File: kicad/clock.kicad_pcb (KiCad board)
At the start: 4 copper layers, 110 x 110 mm, 189 parts, among them J1 GCT_USB4160-03-0230-C_USB_C_V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, J10 JST_ZH_B6B-ZR_1x06_P1.50mm_Ve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, J11 JST_ZH_B2B-ZR_1x02_P1.50mm_Ve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, J2 PinHeader_1x04_P2.54mm_Vertic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, J3 JST_PH_B2B-PH-K_1x02_P2.00mm_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, J6 microSD_HC_Hirose_DM3AT-SF-PE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, J7 JST_ZH_B6B-ZR_1x06_P1.50mm_Ve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, J9 JST_PH_B3B-PH-K_1x03_P2.00mm_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, M1 Juken_X40-879_DualShaft, Q1 SOT-23, Q2 SOT-23, Q3 SOT-23, Q4 SOT-23, Q6 SOT-23, Q7 SOT-23, SW1 SW_SPST_CK_RS282G05A3, SW2 SW_SPST_CK_RS282G05A3, U1 TSSOP-10_3x3mm_P0.5mm, U10 SOT-23-6, U11 SSOP-24_5.3x8.2mm_P0.65mm, U12 SSOP-24_5.3x8.2mm_P0.65mm, U13 SSOP-28_5.3x10.2mm_P0.65mm, U14 OnSemi_QRE1113GR, U15 SOT-23-5, U2 MSOP-12-1EP_3x4.039mm_P0.65mm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, U3 SOT-23-6, U4 SOIC-8_3.9x4.9mm_P1.27mm, U5 SOT-563, U6 SOT-23-5, U7 Texas_HTSSOP-14-1EP_4.4x5mm_P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, U8 ESP32-S3-WROOM-1, U9 HTSSOP-32-1EP_6.1x11mm_P0.65m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, Y1 Crystal_SMD_3215-2Pin_3.2x1.5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

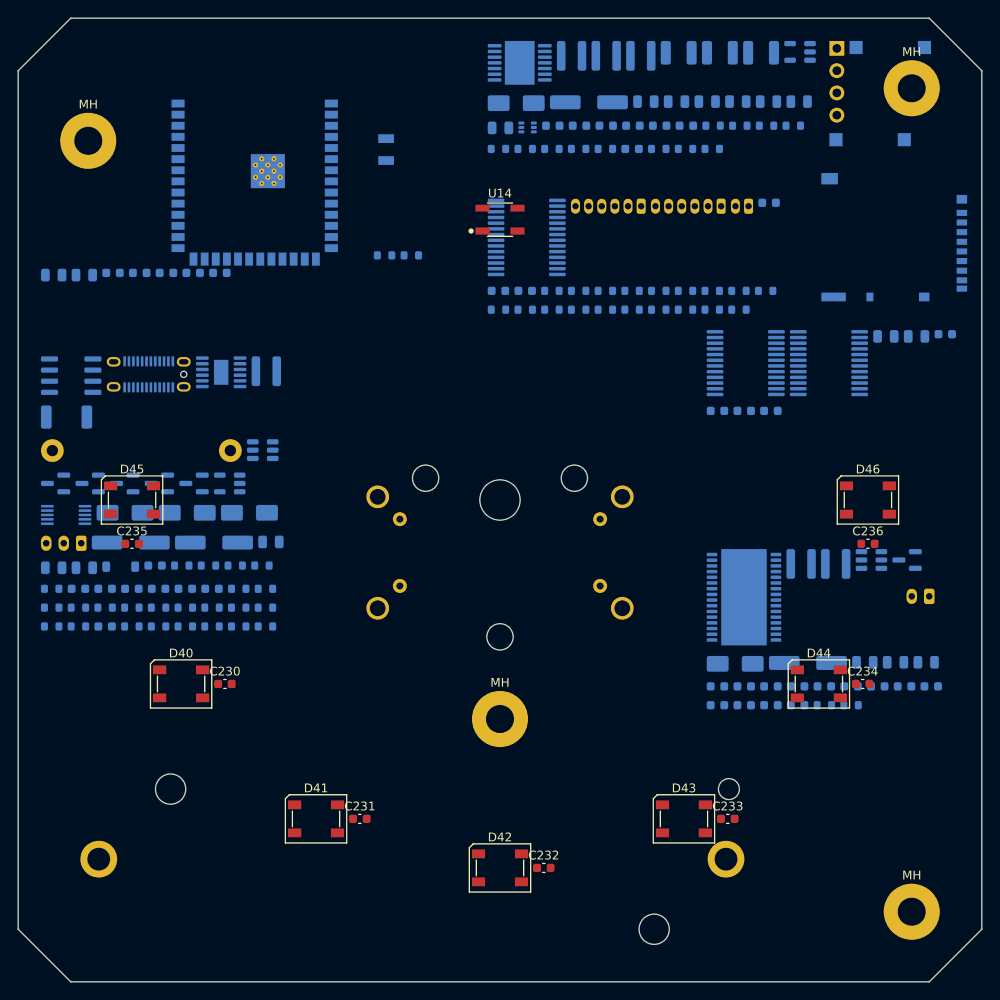
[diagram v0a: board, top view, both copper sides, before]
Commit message: fix PCB layout
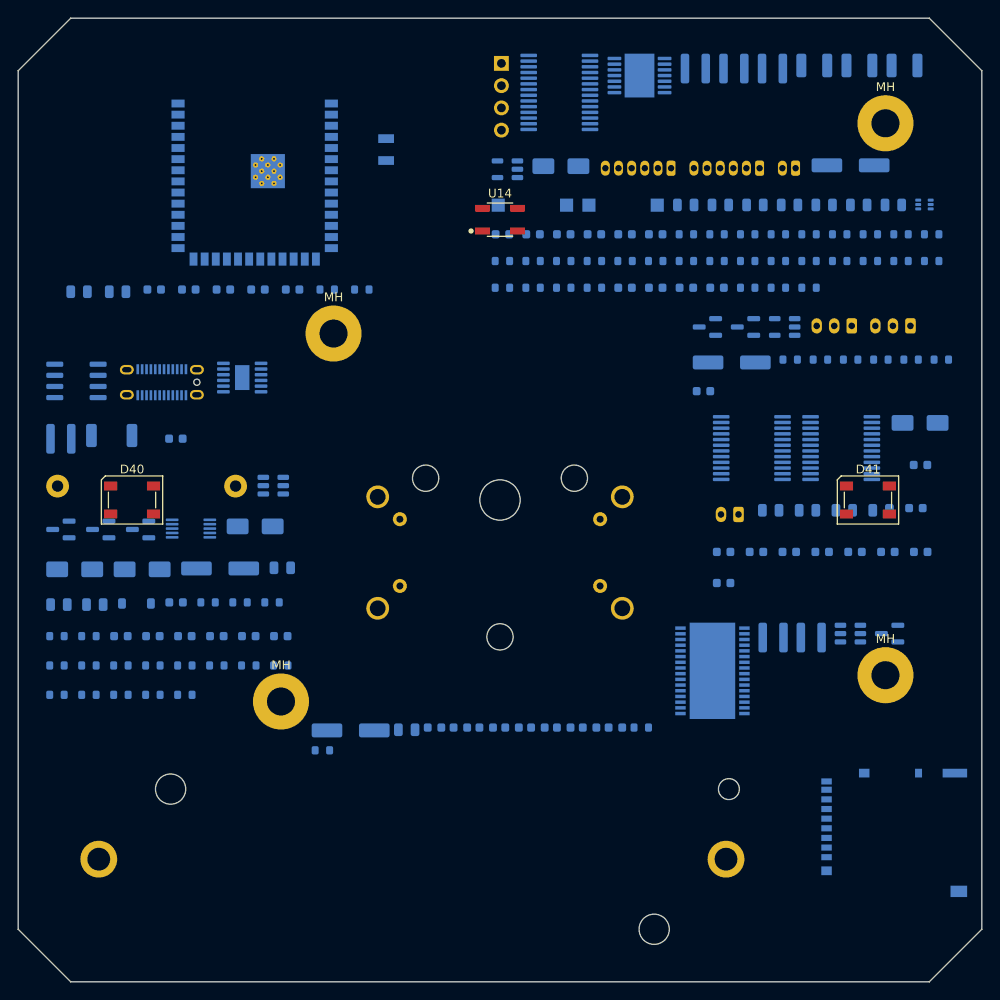
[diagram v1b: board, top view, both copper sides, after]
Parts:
- removed C232, C233, C234, C235, C236: C_0603_1608Metric, C_0603_1608Metric
- removed D42, D43, D44, D45, D46: LED_SK6812_PLCC4_5.0x5.0mm_P3.2mm, LED_SK6812_PLCC4_5.0x5.0mm_P3.2mm
- removed the MH at (8.00, 14.0)
- removed the MH at (102.0, 8.00)
- removed the MH at (55.0, 80.0)
- removed the MH at (102.0, 102.0)
- removed the R97 at (85.3, 31.1)
- removed the R97 at (76.2, 33.3)
- removed the R98 at (54.8, 33.3)
- removed the R98 at (79.2, 33.3)
- removed the R99 at (82.3, 33.3)
- removed the R99 at (57.9, 33.3)
- added J12: JST_PH_B3B-PH-K_1x03_P2.00mm_Vertical, JST_PH_B3B-PH-K_1x03_P2.00mm_Vertical, B.Cu at (101.8, 35.1)
- added MH: MountingHole_3.2mm_M3_Pad, MountingHole_3.2mm_M3_Pad, F.Cu at (36.0, 36.0)
- added MH: MountingHole_3.2mm_M3_Pad, MountingHole_3.2mm_M3_Pad, F.Cu at (99.0, 75.0)
- added MH: MountingHole_3.2mm_M3_Pad, MountingHole_3.2mm_M3_Pad, F.Cu at (30.0, 78.0)
- added MH: MountingHole_3.2mm_M3_Pad, MountingHole_3.2mm_M3_Pad, F.Cu at (99.0, 12.0)
- added R97: R_0603_1608Metric, R_0603_1608Metric, B.Cu at (58.8, 27.7)
- added R97: R_0603_1608Metric, R_0603_1608Metric, B.Cu at (93.8, 27.7)
- added R98: R_0603_1608Metric, R_0603_1608Metric, B.Cu at (97.3, 27.7)
- added R98: R_0603_1608Metric, R_0603_1608Metric, B.Cu at (62.3, 27.7)
- added R99: R_0603_1608Metric, R_0603_1608Metric, B.Cu at (100.8, 27.7)
- added R99: R_0603_1608Metric, R_0603_1608Metric, B.Cu at (65.8, 27.7)
- C230, C231: moved to B.Cu
- moved J9 91.4 mm to (95.1, 35.1)
- moved R110 82.9 mm to (105.4, 39.0)
- moved R107 82.6 mm to (101.9, 39.0)
- moved R106 82.2 mm to (98.5, 39.0)
- moved R105 81.8 mm to (95.0, 39.0)
- moved R104 81.5 mm to (91.6, 39.0)
- moved R52 81.1 mm to (88.1, 39.0)
- moved C231 75.7 mm to (103.0, 51.0), turned to 180 degrees
- moved C238 73.4 mm to (78.2, 42.6)
- moved D41 72.8 mm to (97.0, 55.0)
- moved J6 68.0 mm to (100.0, 93.0), turned to -90 degrees
- moved U15 65.8 mm to (87.5, 35.2)
- moved Q7 65.4 mm to (83.0, 35.2)
- moved Q6 65.0 mm to (78.7, 35.2)
- moved C237 62.6 mm to (81.5, 39.3)
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
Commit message: pcb creation
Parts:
- removed MH (x4): MountingHole_3.2mm_M3_Pad, MountingHole_3.2mm_M3_Pad
- removed the R97 at (58.8, 27.7)
- removed the R97 at (93.8, 27.7)
- removed the R98 at (97.3, 27.7)
- removed the R98 at (62.3, 27.7)
- removed the R99 at (100.8, 27.7)
- removed the R99 at (65.8, 27.7)
- added C163: C_0603_1608Metric, C_0603_1608Metric, B.Cu at (84.8, 75.9)
- added D13: D_SOD-123, D_SOD-123, B.Cu at (99.1, 104.3)
- added H1: MountingHole_3.2mm_M3_Pad, MountingHole_3.2mm_M3_Pad, F.Cu at (5.00, 5.00)
- added H2: MountingHole_3.2mm_M3_Pad, MountingHole_3.2mm_M3_Pad, F.Cu at (104.8, 5.20)
- added H3: MountingHole_3.2mm_M3_Pad, MountingHole_3.2mm_M3_Pad, F.Cu at (5.00, 105.0)
- added H4: MountingHole_3.2mm_M3_Pad, MountingHole_3.2mm_M3_Pad, F.Cu at (105.5, 105.5)
- added Q8: SOT-23, SOT-23, B.Cu at (100.8, 97.3)
- added Q9: SOT-23, SOT-23, B.Cu at (96.7, 97.3)
- added R24: R_0603_1608Metric, R_0603_1608Metric, B.Cu at (93.4, 61.4)
- added R25: R_0603_1608Metric, R_0603_1608Metric, B.Cu at (95.5, 104.5)
- added R26: R_0603_1608Metric, R_0603_1608Metric, B.Cu at (96.3, 107.9)
- added R27: R_0603_1608Metric, R_0603_1608Metric, B.Cu at (92.7, 108.1)
- added R63: R_0603_1608Metric, R_0603_1608Metric, B.Cu at (85.0, 29.0)
- added R97: R_0603_1608Metric, R_0603_1608Metric, B.Cu at (89.5, 13.8)
- added R98: R_0603_1608Metric, R_0603_1608Metric, B.Cu at (50.4, 31.8)
- added R99: R_0603_1608Metric, R_0603_1608Metric, B.Cu at (54.1, 31.8)
- added U16: SOT-23-6, SOT-23-6, B.Cu at (87.0, 23.7)
- C230, C231: moved to F.Cu
- U1: value TSSOP-10_3x3mm_P0.5mm -> SSOP-10-1EP_3.9x4.9mm_P1mm_EP2.1x3.3mm; footprint TSSOP-10_3x3mm_P0.5mm -> SSOP-10-1EP_3.9x4.9mm_P1mm_EP2.1x3.3mm
- moved C101 103.5 mm to (104.0, 38.1), turned to -90 degrees
- moved R10 103.1 mm to (103.7, 46.0)
- moved J6 103.0 mm to (13.5, 37.0), turned to 90 degrees
- moved R11 97.8 mm to (102.5, 48.3)
- moved C102 96.6 mm to (104.0, 42.0), turned to -90 degrees
- moved C125 95.5 mm to (9.50, 69.5)
- moved U5 95.2 mm to (14.0, 54.0)
- moved R13 94.6 mm to (106.6, 48.5), turned to -90 degrees
- moved R12 93.8 mm to (102.5, 50.4)
- moved R4 92.2 mm to (92.5, 43.3)
- moved Q2 91.5 mm to (92.6, 96.5), turned to -90 degrees
- moved Q3 91.2 mm to (92.5, 104.7), turned to -90 degrees
- moved R43 90.7 mm to (10.0, 73.0)
- moved R19 90.7 mm to (92.0, 100.6), turned to -90 degrees
- moved D12 90.2 mm to (99.2, 92.9)
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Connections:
- J1 pad A6: USB_DP -> Net-(J1-D+-PadA6)
- J1 pad A7: USB_DM -> Net-(J1-D--PadA7)
- J1 pad B6: USB_DP -> Net-(J1-D+-PadA6)
- J1 pad B7: USB_DM -> Net-(J1-D--PadA7)
- U13 pad 8: unconnected-(U13-GPB7-Pad8) -> CELL_TEST
- U7 pad 11: unconnected-(U7-NC-Pad11) -> GND
- U7 pad 7: Net-(U7-COMP) -> GND
- U7 pad 8: GND -> Net-(U7-COMP)
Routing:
- added copper zone on B.Cu, net GND
- added copper zone on F.Cu, net GND
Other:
- board text added: "12V"
- board text added: "3V3"
- board text added: "5V"
- board text added: "AUDIO"
- board text added: "CELL+"
- board text added: "CELL-"
- board text added: "CHARGER"
- board text added: "IO-EXP"
- board text added: "PROTECT"
- board text added: "USB-PD"
- board text added: "WAKE"
- board text added: "clock v0.19"
- board text added: "wooden clock v0.19 2026-07-22"

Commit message: add datasheet and review schematics
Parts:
- BT1: value BatteryHolder_Keystone_1043_1x18650 -> 18650 (Keystone 1043); footprint BatteryHolder_Keystone_1043_1x18650 -> clock:BatteryHolder_Keystone_1043_1x18650
- C1, C108, C144, C160, C165, C167, C171: value C_0603_1608Metric -> 1uF; footprint C_0603_1608Metric -> Capacitor_SMD:C_0603_1608Metric
- C100, C101, C106, C120, C124, C127, C140, C162, C200, C210, C222: value C_0805_2012Metric -> 10uF; footprint C_0805_2012Metric -> Capacitor_SMD:C_0805_2012Metric
- C102, C104, C109, C110, C128, C134, C142, C143, C161, C163, C164, C166, C170, C186, C201, C202, C211, C212, C223, C230, C231, C238, C239, C240, C241: value C_0603_1608Metric -> 100nF; footprint C_0603_1608Metric -> Capacitor_SMD:C_0603_1608Metric
- C105: value C_0603_1608Metric -> 22pF; footprint C_0603_1608Metric -> Capacitor_SMD:C_0603_1608Metric
- C107, C129, C237: value CP_Elec_6.3x7.7 -> 100uF; footprint CP_Elec_6.3x7.7 -> Capacitor_SMD:CP_Elec_6.3x7.7
- C121, C122, C125, C141: value C_0805_2012Metric -> 22uF; footprint C_0805_2012Metric -> Capacitor_SMD:C_0805_2012Metric
- C123: value C_0603_1608Metric -> 220pF; footprint C_0603_1608Metric -> Capacitor_SMD:C_0603_1608Metric
- C126: value C_0603_1608Metric -> 6.8pF; footprint C_0603_1608Metric -> Capacitor_SMD:C_0603_1608Metric
- C130, C131, C132: value C_1210_3225Metric -> 22uF; footprint C_1210_3225Metric -> Capacitor_SMD:C_1210_3225Metric
- C133: value C_0603_1608Metric -> 47nF; footprint C_0603_1608Metric -> Capacitor_SMD:C_0603_1608Metric
- C135: value C_0603_1608Metric -> 100pF; footprint C_0603_1608Metric -> Capacitor_SMD:C_0603_1608Metric
- C145, C146: value C_0603_1608Metric -> 18pF; footprint C_0603_1608Metric -> Capacitor_SMD:C_0603_1608Metric
- C172: value CP_Elec_6.3x7.7 -> 220uF; footprint CP_Elec_6.3x7.7 -> Capacitor_SMD:CP_Elec_6.3x7.7
- C180, C181, C182, C183: value C_0603_1608Metric -> 220nF; footprint C_0603_1608Metric -> Capacitor_SMD:C_0603_1608Metric
- C184, C185: value C_0805_2012Metric -> 0.68uF; footprint C_0805_2012Metric -> Capacitor_SMD:C_0805_2012Metric
- D1: value D_SMA -> SMAJ22CA; footprint D_SMA -> Diode_SMD:D_SMA
- D10: value D_SOD-123 -> BAT46; footprint D_SOD-123 -> Diode_SMD:D_SOD-123
- D11, D20: value D_SMA -> B340A; footprint D_SMA -> Diode_SMD:D_SMA
- D12: value D_SMA -> SMAJ5.0CA; footprint D_SMA -> Diode_SMD:D_SMA
- D13: value D_SOD-123 -> BAT42W; footprint D_SOD-123 -> Diode_SMD:D_SOD-123
- D30: value D_SMA -> SS34; footprint D_SMA -> Diode_SMD:D_SMA
- D40, D41: value LED_SK6812_PLCC4_5.0x5.0mm_P3.2mm -> SK6812RGBW; footprint LED_SK6812_PLCC4_5.0x5.0mm_P3.2mm -> LED_SMD:LED_SK6812_PLCC4_5.0x5.0mm_P3.2mm
- F1: value Fuse_TCO_Cantherm_SDF_L10.5mm_D4.0mm_P20.32mm_Horizontal -> TCO 77C; footprint Fuse_TCO_Cantherm_SDF_L10.5mm_D4.0mm_P20.32mm_Horizontal -> clock:Fuse_TCO_Cantherm_SDF_L10.5mm_D4.0mm_P20.32mm_Horizontal
- J1: value GCT_USB4160-03-0230-C_USB_C_Vertical -> USB4160-03-0230-C; footprint GCT_USB4160-03-0230-C_USB_C_Vertical -> clock:GCT_USB4160-03-0230-C_USB_C_Vertical
- J10: value JST_ZH_B6B-ZR_1x06_P1.50mm_Vertical -> Knob: EM14 enc+SW (top face); footprint JST_ZH_B6B-ZR_1x06_P1.50mm_Vertical -> Connector_JST:JST_ZH_B6B-ZR_1x06_P1.50mm_Vertical
- J11: value JST_ZH_B2B-ZR_1x02_P1.50mm_Vertical -> Radio-off toggle (rear); footprint JST_ZH_B2B-ZR_1x02_P1.50mm_Vertical -> Connector_JST:JST_ZH_B2B-ZR_1x02_P1.50mm_Vertical
- J12: value JST_PH_B3B-PH-K_1x03_P2.00mm_Vertical -> NeoPixel ext (5V/DATA/GND, pos 3-7); footprint JST_PH_B3B-PH-K_1x03_P2.00mm_Vertical -> Connector_JST:JST_PH_B3B-PH-K_1x03_P2.00mm_Vertical
- J2: value PinHeader_1x04_P2.54mm_Vertical -> PROG; footprint PinHeader_1x04_P2.54mm_Vertical -> Connector_PinHeader_2.54mm:PinHeader_1x04_P2.54mm_Vertical
- J3: value JST_PH_B2B-PH-K_1x02_P2.00mm_Vertical -> Speaker DMA58-4 (4R); footprint JST_PH_B2B-PH-K_1x02_P2.00mm_Vertical -> Connector_JST:JST_PH_B2B-PH-K_1x02_P2.00mm_Vertical
- J6: value microSD_HC_Hirose_DM3AT-SF-PEJM5 -> DM3AT-SF-PEJM5; footprint microSD_HC_Hirose_DM3AT-SF-PEJM5 -> Connector_Card:microSD_HC_Hirose_DM3AT-SF-PEJM5
- J7: value JST_ZH_B6B-ZR_1x06_P1.50mm_Vertical -> Sensor board (BME688+TSL2591+LIS3DH); footprint JST_ZH_B6B-ZR_1x06_P1.50mm_Vertical -> Connector_JST:JST_ZH_B6B-ZR_1x06_P1.50mm_Vertical
- J9: value JST_PH_B3B-PH-K_1x03_P2.00mm_Vertical -> Wake COB 12V (warm+cool); footprint JST_PH_B3B-PH-K_1x03_P2.00mm_Vertical -> Connector_JST:JST_PH_B3B-PH-K_1x03_P2.00mm_Vertical
- L1, L5, L6: value L_Coilcraft_XAL4030-XXX -> 10uH; footprint L_Coilcraft_XAL4030-XXX -> Inductor_SMD:L_Coilcraft_XAL4030-XXX
- L2: value L_Coilcraft_XAL4020-XXX -> 1uH; footprint L_Coilcraft_XAL4020-XXX -> Inductor_SMD:L_Coilcraft_XAL4020-XXX
- L3: value L_Coilcraft_XAL4020-XXX -> 2.2uH; footprint L_Coilcraft_XAL4020-XXX -> Inductor_SMD:L_Coilcraft_XAL4020-XXX
- L4: value L_Coilcraft_XAL4030-XXX -> 4.7uH; footprint L_Coilcraft_XAL4030-XXX -> Inductor_SMD:L_Coilcraft_XAL4030-XXX
- M1: value Juken_X40-879_DualShaft -> X40.879; footprint Juken_X40-879_DualShaft -> clock:Juken_X40-879_DualShaft
- Q1, Q3, Q8: value SOT-23 -> 2N7002; footprint SOT-23 -> Package_TO_SOT_SMD:SOT-23
- Q2, Q4, Q9: value SOT-23 -> AO3401A; footprint SOT-23 -> Package_TO_SOT_SMD:SOT-23
- Q6, Q7: value SOT-23 -> AO3400A; footprint SOT-23 -> Package_TO_SOT_SMD:SOT-23
- R1: value R_0603_1608Metric -> 1k; footprint R_0603_1608Metric -> Resistor_SMD:R_0603_1608Metric
- R10: value R_0603_1608Metric -> 316k; footprint R_0603_1608Metric -> Resistor_SMD:R_0603_1608Metric
- R104, R106, R20: value R_0603_1608Metric -> 100R; footprint R_0603_1608Metric -> Resistor_SMD:R_0603_1608Metric
- R105, R107, R113, R12, R13, R2, R4, R46, R50, R51, R52, R60, R62, R70, R71, R72, R93, R94, R97, R99, RT1: value R_0603_1608Metric -> 10k; footprint R_0603_1608Metric -> Resistor_SMD:R_0603_1608Metric
- R11, R111, R112, R19, R22, R23, R24, R25, R26, R27, R41, R43, R44, R63: value R_0603_1608Metric -> 100k; footprint R_0603_1608Metric -> Resistor_SMD:R_0603_1608Metric
- R110: value R_0603_1608Metric -> 330R; footprint R_0603_1608Metric -> Resistor_SMD:R_0603_1608Metric
- R114, R115, R15: value R_0603_1608Metric -> 200k; footprint R_0603_1608Metric -> Resistor_SMD:R_0603_1608Metric
- R14: value R_0603_1608Metric -> 45.3k; footprint R_0603_1608Metric -> Resistor_SMD:R_0603_1608Metric
- R16: value R_0603_1608Metric -> 976k; footprint R_0603_1608Metric -> Resistor_SMD:R_0603_1608Metric
- R17: value R_0603_1608Metric -> 909R; footprint R_0603_1608Metric -> Resistor_SMD:R_0603_1608Metric
- R18: value R_2010_5025Metric -> 0.1R 1W; footprint R_2010_5025Metric -> Resistor_SMD:R_2010_5025Metric
- R21: value R_0603_1608Metric -> 2k; footprint R_0603_1608Metric -> Resistor_SMD:R_0603_1608Metric
- R3: value R_0603_1608Metric -> 56k; footprint R_0603_1608Metric -> Resistor_SMD:R_0603_1608Metric
- R40: value R_0603_1608Metric -> 732k; footprint R_0603_1608Metric -> Resistor_SMD:R_0603_1608Metric
- R42: value R_0603_1608Metric -> 453k; footprint R_0603_1608Metric -> Resistor_SMD:R_0603_1608Metric
- R45: value R_0603_1608Metric -> 86.6k; footprint R_0603_1608Metric -> Resistor_SMD:R_0603_1608Metric
- R47: value R_0603_1608Metric -> 95.3k; footprint R_0603_1608Metric -> Resistor_SMD:R_0603_1608Metric
- R48: value R_0603_1608Metric -> 2.55k; footprint R_0603_1608Metric -> Resistor_SMD:R_0603_1608Metric
- R61, R90, R91, R92: value R_0603_1608Metric -> 0R; footprint R_0603_1608Metric -> Resistor_SMD:R_0603_1608Metric
- R95, R96: value R_0603_1608Metric -> 4.7k; footprint R_0603_1608Metric -> Resistor_SMD:R_0603_1608Metric
- R98: value R_0603_1608Metric -> 150R; footprint R_0603_1608Metric -> Resistor_SMD:R_0603_1608Metric
- SW1: value SW_SPST_CK_RS282G05A3 -> RESET; footprint SW_SPST_CK_RS282G05A3 -> Button_Switch_SMD:SW_SPST_CK_RS282G05A3
- SW2: value SW_SPST_CK_RS282G05A3 -> BOOT; footprint SW_SPST_CK_RS282G05A3 -> Button_Switch_SMD:SW_SPST_CK_RS282G05A3
- U1: value SSOP-10-1EP_3.9x4.9mm_P1mm_EP2.1x3.3mm -> CH224K; footprint SSOP-10-1EP_3.9x4.9mm_P1mm_EP2.1x3.3mm -> Package_SO:SSOP-10-1EP_3.9x4.9mm_P1mm_EP2.1x3.3mm
- U10: value SOT-23-6 -> LTC4412ES6; footprint SOT-23-6 -> Package_TO_SOT_SMD:SOT-23-6
- U11, U12: value SSOP-24_5.3x8.2mm_P0.65mm -> TB6612FNG; footprint SSOP-24_5.3x8.2mm_P0.65mm -> Package_SO:SSOP-24_5.3x8.2mm_P0.65mm
- U13: value SSOP-28_5.3x10.2mm_P0.65mm -> MCP23017; footprint SSOP-28_5.3x10.2mm_P0.65mm -> Package_SO:SSOP-28_5.3x10.2mm_P0.65mm
- U14: value OnSemi_QRE1113GR -> QRE1113GR; footprint OnSemi_QRE1113GR -> clock:OnSemi_QRE1113GR
- U15: value SOT-23-5 -> SN74AHCT1G125; footprint SOT-23-5 -> Package_TO_SOT_SMD:SOT-23-5
- U16: value SOT-23-6 -> USBLC6-2SC6; footprint SOT-23-6 -> Package_TO_SOT_SMD:SOT-23-6
- U2: value MSOP-12-1EP_3x4.039mm_P0.65mm_EP1.651x2.845mm -> LT3652EMSE; footprint MSOP-12-1EP_3x4.039mm_P0.65mm_EP1.651x2.845mm -> Package_SO:MSOP-12-1EP_3x4.039mm_P0.65mm_EP1.651x2.845mm
- U3: value SOT-23-6 -> HY2111-GB; footprint SOT-23-6 -> Package_TO_SOT_SMD:SOT-23-6
- U4: value SOIC-8_3.9x4.9mm_P1.27mm -> AOSD32334C; footprint SOIC-8_3.9x4.9mm_P1.27mm -> Package_SO:SOIC-8_3.9x4.9mm_P1.27mm
- U5: value SOT-563 -> TPS61023; footprint SOT-563 -> Package_TO_SOT_SMD:SOT-563
- U6: value SOT-23-5 -> TLV62569DBVR; footprint SOT-23-5 -> Package_TO_SOT_SMD:SOT-23-5
- U7: value Texas_HTSSOP-14-1EP_4.4x5mm_P0.65mm_EP3.4x5mm_Mask3.155x3.255mm -> TPS55340PWPR; footprint Texas_HTSSOP-14-1EP_4.4x5mm_P0.65mm_EP3.4x5mm_Mask3.155x3.255mm -> Package_SO:Texas_HTSSOP-14-1EP_4.4x5mm_P0.65mm_EP3.4x5mm_Mask3.155x3.255mm
- U8: value ESP32-S3-WROOM-1 -> ESP32-S3-WROOM-1-N16R8; footprint ESP32-S3-WROOM-1 -> RF_Module:ESP32-S3-WROOM-1
- U9: value HTSSOP-32-1EP_6.1x11mm_P0.65mm_EP5.2x11mm_Mask4.11x4.36mm -> TAS5760MDAPR; footprint HTSSOP-32-1EP_6.1x11mm_P0.65mm_EP5.2x11mm_Mask4.11x4.36mm -> Package_SO:HTSSOP-32-1EP_6.1x11mm_P0.65mm_EP5.2x11mm_Mask4.11x4.36mm
- Y1: value Crystal_SMD_3215-2Pin_3.2x1.5mm -> 32.768kHz; footprint Crystal_SMD_3215-2Pin_3.2x1.5mm -> Crystal:Crystal_SMD_3215-2Pin_3.2x1.5mm

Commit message: schematic verification pass
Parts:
- D30: value SS34 -> B340A
- L4: footprint Inductor_SMD:L_Coilcraft_XAL4030-XXX -> Inductor_SMD:L_Coilcraft_XAL5050-XXX
- moved Q1 1.33 mm to (91.4, 61.2)
- moved R24 1.29 mm to (94.5, 62.0)
- moved R15 1.29 mm to (90.4, 57.0)
- moved L4 1.25 mm to (83.9, 58.7)
- moved R16 1.21 mm to (88.3, 60.4)
- moved R14 1.19 mm to (88.3, 56.8)
- moved C105 1.08 mm to (92.6, 57.0)
- moved C106 1.04 mm to (84.4, 53.3)
- moved C201 1.04 mm to (83.1, 50.1)
- moved C200 0.88 mm to (83.1, 47.7)
- moved R44 0.60 mm to (77.9, 58.5)
- moved D20 0.46 mm to (85.4, 64.3)
- moved C127 0.36 mm to (85.8, 68.3)
- moved U7 0.34 mm to (76.3, 64.8)
- moved R18 0.32 mm to (89.2, 53.1)
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
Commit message: cosmetic changes in builder
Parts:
- removed R52: 10k, Resistor_SMD:R_0603_1608Metric

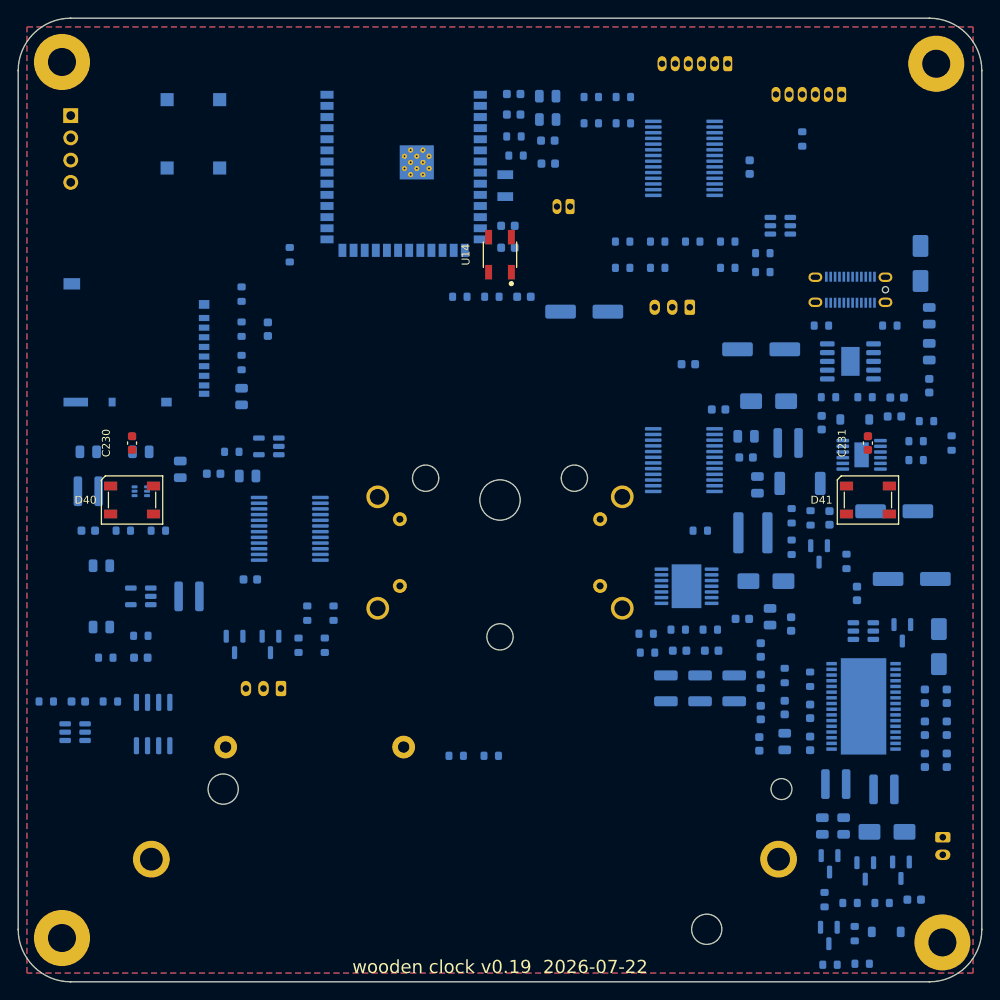
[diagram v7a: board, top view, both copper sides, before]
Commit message: autorouter
routed all except 1 `SPK_FAULT`
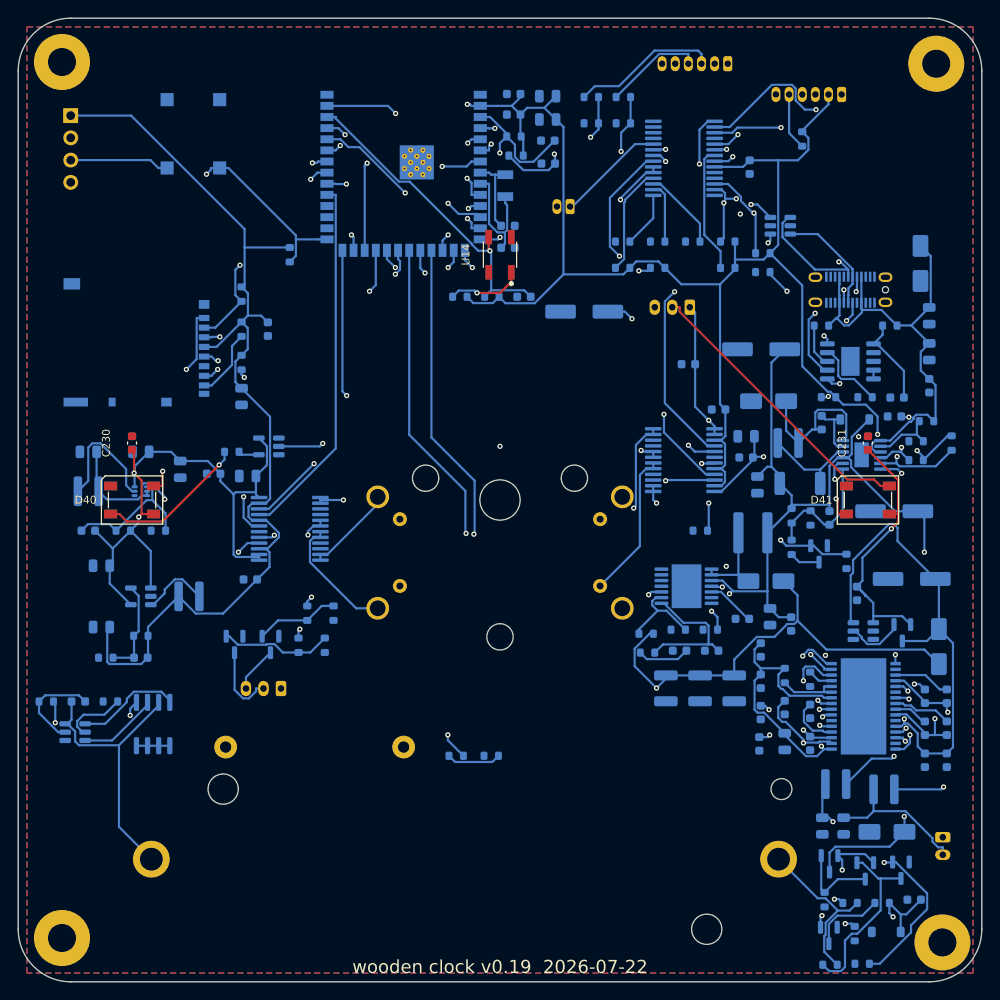
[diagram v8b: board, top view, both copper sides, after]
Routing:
- net +3V3: track 0.00 -> 409.2 mm, vias 0 -> 4
- net +5V: track 0.00 -> 260.9 mm, vias 0 -> 6
- net VBAT: track 0.00 -> 207.5 mm, vias 0 -> 4
- net VBAT_SENSE: track 0.00 -> 141.9 mm, vias 0 -> 3
- net I2C_SDA: track 0.00 -> 133.2 mm, vias 0 -> 5
- net I2C_SCL: track 0.00 -> 125.0 mm, vias 0 -> 3
- net Net-(BT1-Pin_1): track 0.00 -> 124.9 mm, vias 0 -> 2
- net Net-(U8-IO43_MCLK): track 0.00 -> 113.7 mm, vias 0 -> 3
- net CELL_TEST: track 0.00 -> 108.0 mm, vias 0 -> 2
- net VBAT_DIV_EN: track 0.00 -> 100.7 mm, vias 0 -> 3
- net STEP_STBY: track 0.00 -> 98.3 mm, vias 0 -> 3
- net +12V: track 0.00 -> 95.2 mm, vias 0 -> 1
- net SPK_SD: track 0.00 -> 89.1 mm, vias 0 -> 3
- net Net-(U8-IO11_LRCLK): track 0.00 -> 87.7 mm, vias 0 -> 3
- net Net-(D40-DOUT): track 0.00 -> 85.2 mm, vias 0 -> 2
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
